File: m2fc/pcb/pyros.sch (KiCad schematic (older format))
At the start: 48 parts, among them P601 CONN_2, P602 CONN_2, P603 CONN_2, Q601 MOSFET_P, Q602 MOSFET_N, Q603 MOSFET_P, Q604 MOSFET_N, Q605 MOSFET_P, Q606 MOSFET_N, U601 HOUSING, U602 HOUSING, U603 HOUSING

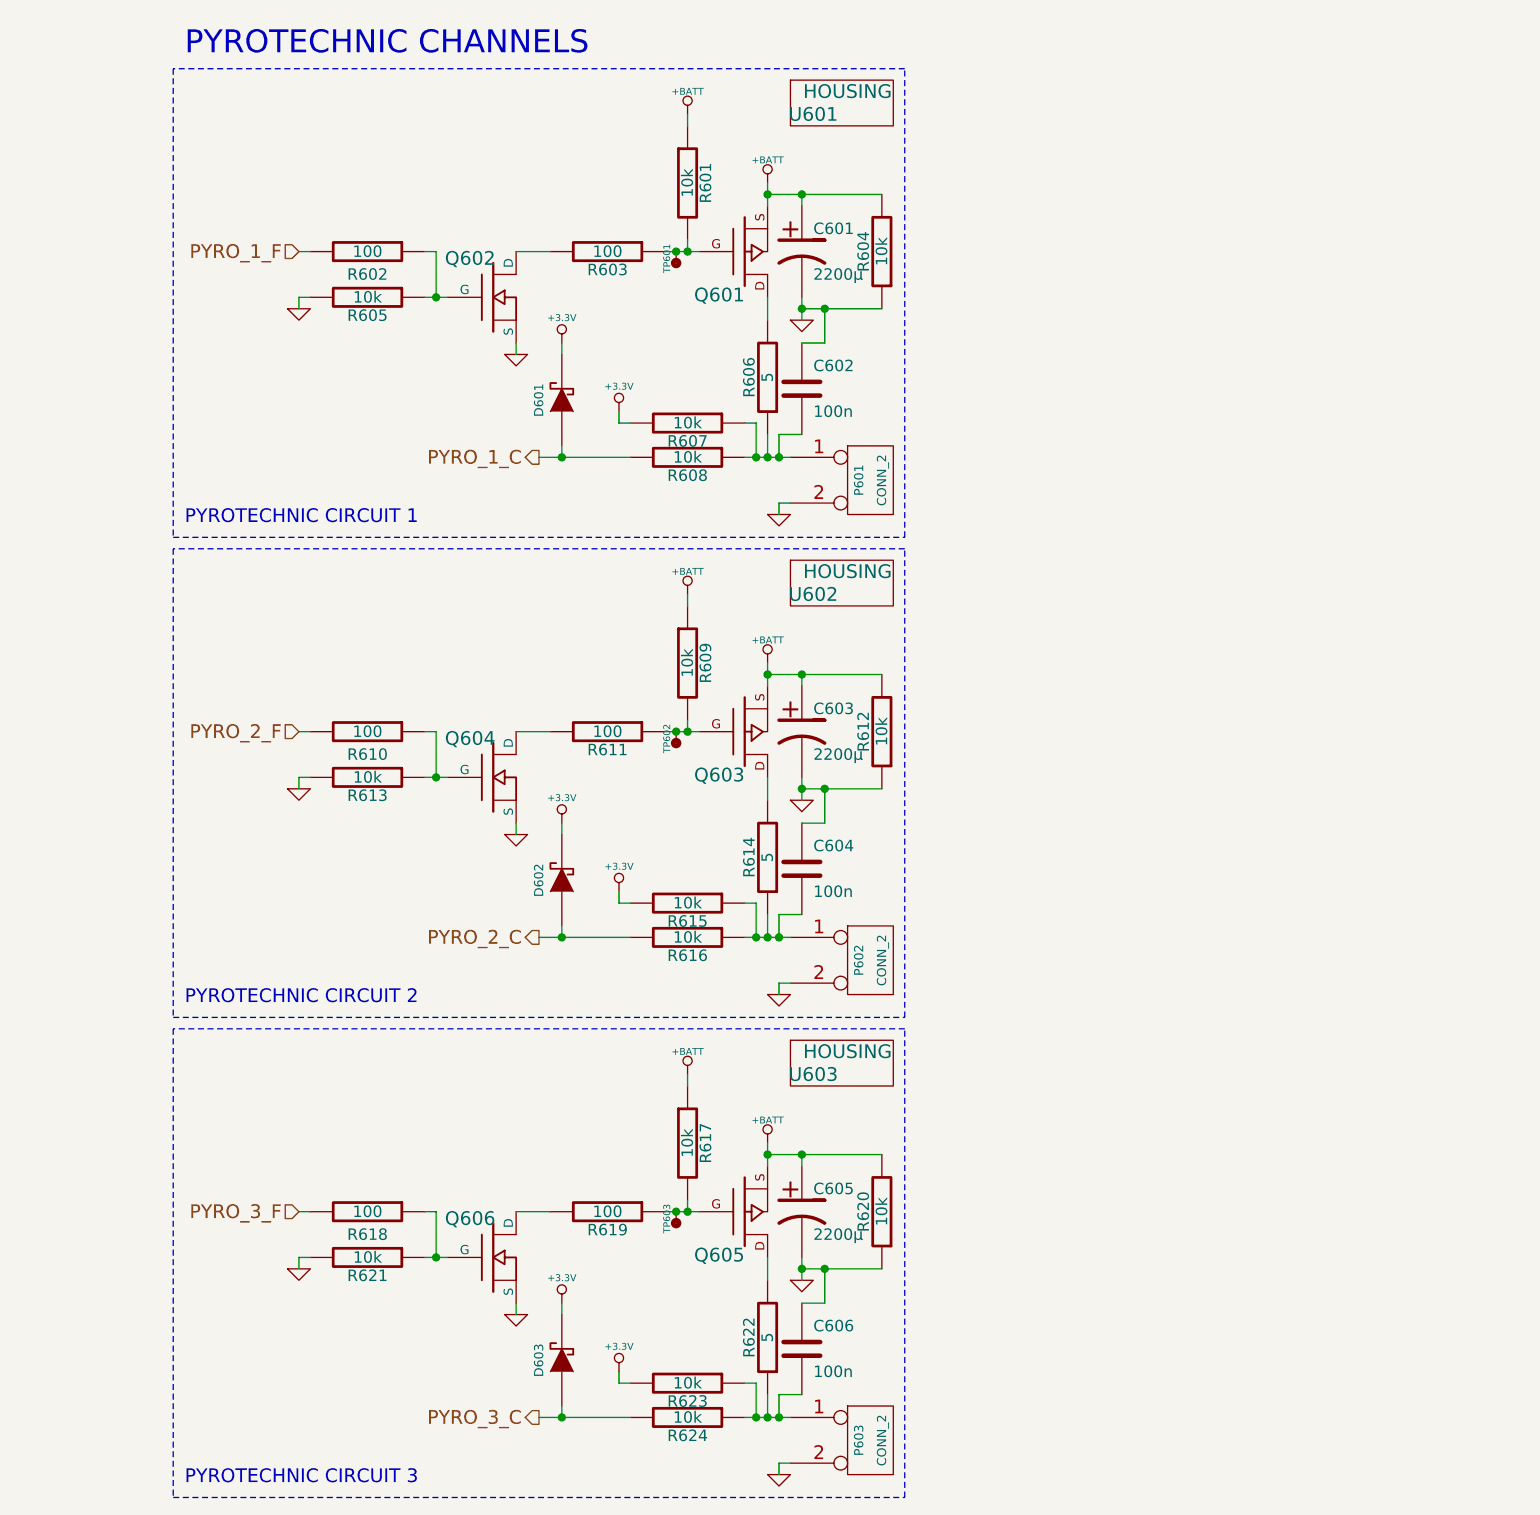
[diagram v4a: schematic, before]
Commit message: sd pullups, shielded sgs
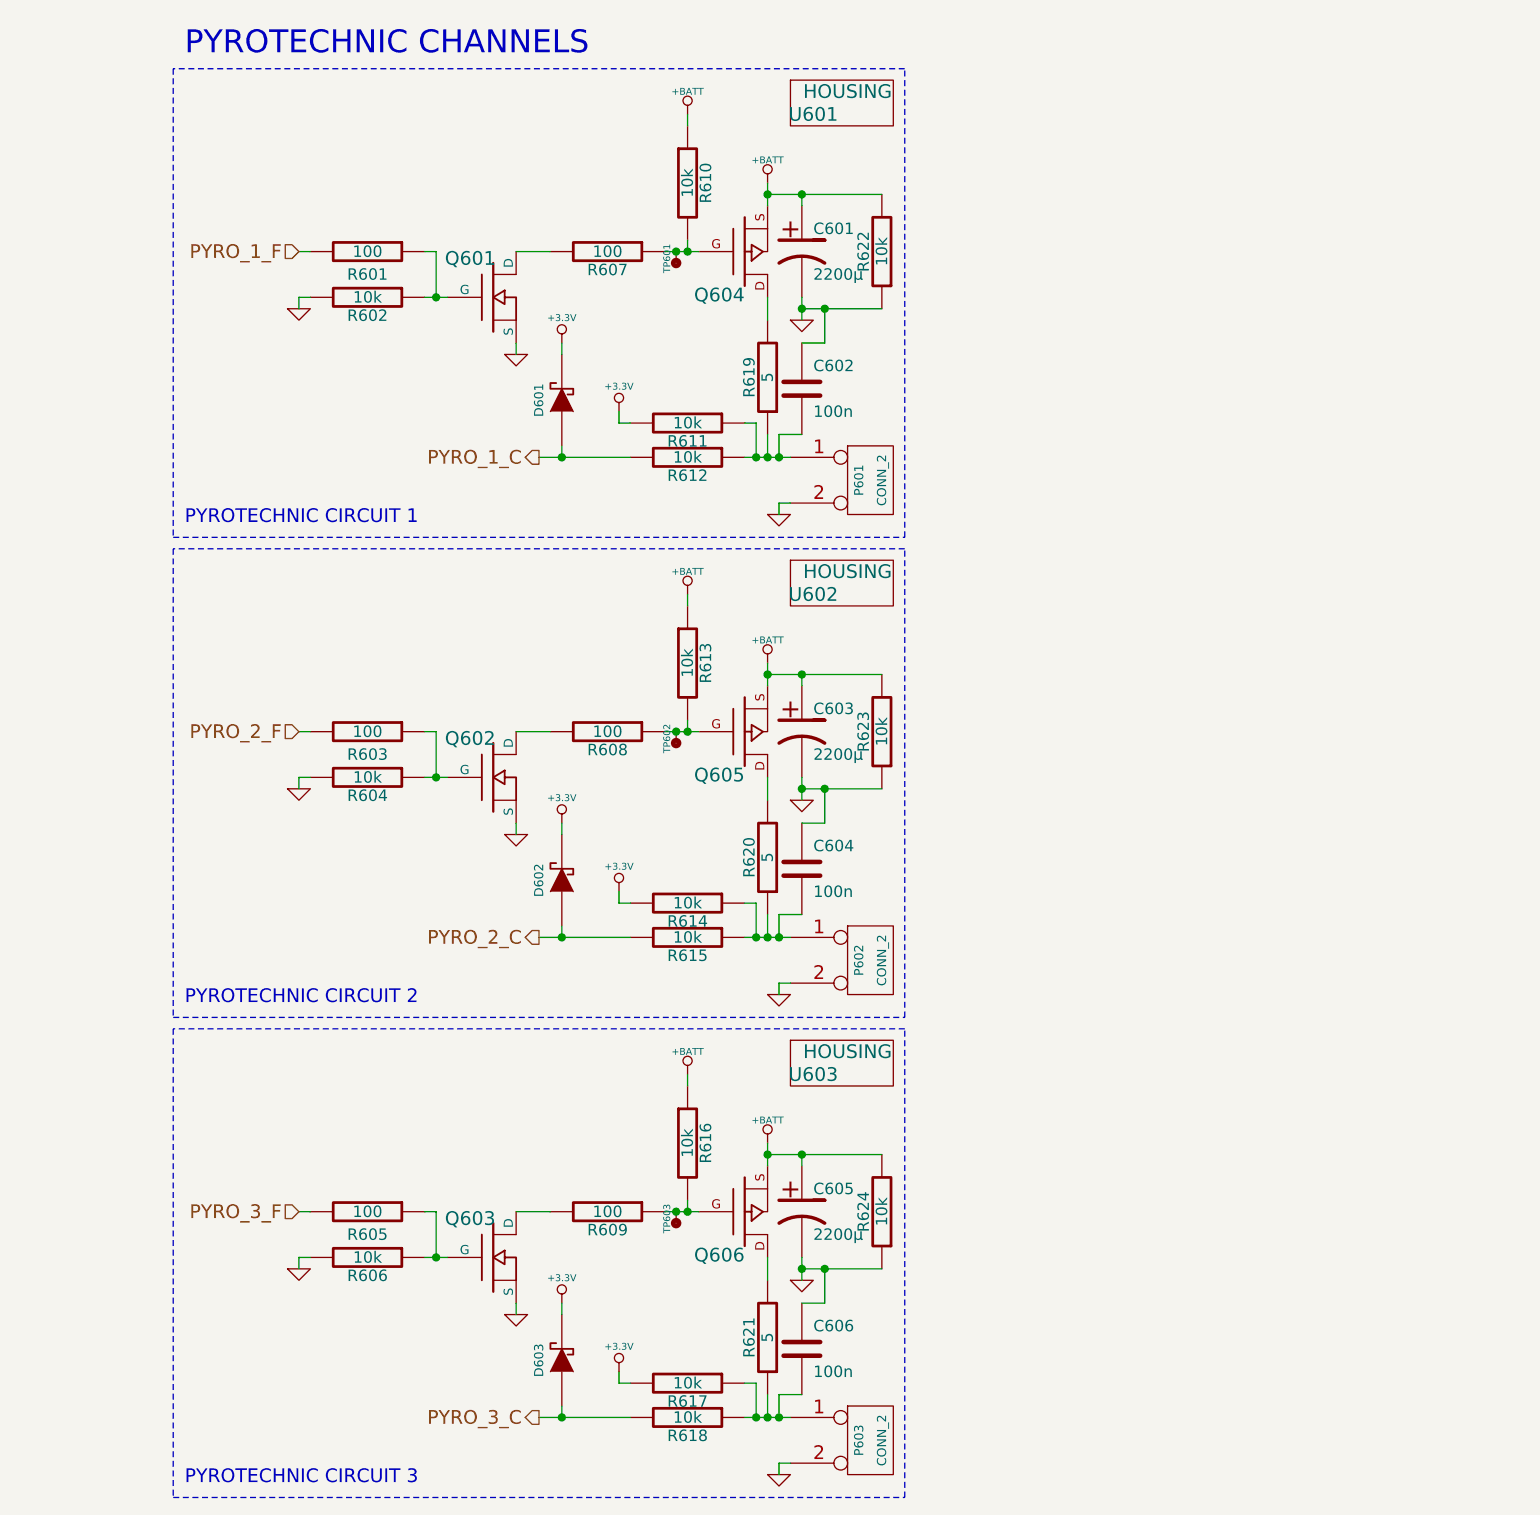
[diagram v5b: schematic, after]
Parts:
- C602, C604, C606: footprint 0603 -> m2fc:C0603
- P601, P602, P603: footprint (none) -> m2fc:S02B-PASK-2
- R601: renamed from R602; footprint 0603 -> m2fc:R0603
- R602: renamed from R605; footprint 0603 -> m2fc:R0603
- R603: renamed from R610; footprint 0603 -> m2fc:R0603
- R604: renamed from R613; footprint 0603 -> m2fc:R0603
- R605: renamed from R618; footprint 0603 -> m2fc:R0603
- R606: renamed from R621; footprint 0603 -> m2fc:R0603
- R607: renamed from R603; footprint 0603 -> m2fc:R0603
- R608: renamed from R611; footprint 0603 -> m2fc:R0603
- R609: renamed from R619; footprint 0603 -> m2fc:R0603
- R610: renamed from R601; footprint 0603 -> m2fc:R0603
- R611: renamed from R607; footprint 0603 -> m2fc:R0603
- R612: renamed from R608; footprint 0603 -> m2fc:R0603
- R613: renamed from R609; footprint 0603 -> m2fc:R0603
- R614: renamed from R615; footprint 0603 -> m2fc:R0603
- R615: renamed from R616; footprint 0603 -> m2fc:R0603
- R616: renamed from R617; footprint 0603 -> m2fc:R0603
- R617: renamed from R623; footprint 0603 -> m2fc:R0603
- R618: renamed from R624; footprint 0603 -> m2fc:R0603
- R622: renamed from R604; footprint 0603 -> m2fc:R0603
- R623: renamed from R612; footprint 0603 -> m2fc:R0603
- R624: renamed from R620; footprint 0603 -> m2fc:R0603
- TP601, TP602, TP603: footprint (none) -> m2fc:TESTPAD
- renumbered Q602 to Q601, Q604 to Q602, Q606 to Q603, Q601 to Q604, Q603 to Q605, Q605 to Q606, R606 to R619, R614 to R620, R622 to R621

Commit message: add esd diodes to m2fc
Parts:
- added D502, D504, D506: CGA0402MLC-12G, m2fc:R0402, symbol CGA0402MLC-12G
- renumbered C601 to C501, C602 to C502, C603 to C503, C604 to C504, C605 to C505, C606 to C506, D601 to D501, D602 to D503, D603 to D505, P601 to P501, P602 to P502, P603 to P503, Q604 to Q501, Q601 to Q502, Q605 to Q503, Q602 to Q504, Q606 to Q505, Q603 to Q506, R610 to R501, R601 to R502, R607 to R503, R622 to R504, R602 to R505, R619 to R506, R611 to R507, R612 to R508, R613 to R509, R603 to R510, R608 to R511, R623 to R512, R604 to R513, R620 to R514, R614 to R515, R615 to R516, R616 to R517, R605 to R518, R609 to R519, R624 to R520, R606 to R521, R621 to R522, R617 to R523, R618 to R524, TP601 to TP501, TP602 to TP502, TP603 to TP503, U601 to U501, U602 to U502, U603 to U503
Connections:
- net GND: now also D502.2, D504.2, D506.2
- net at C502.2, P501.1 (P1), R506.1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: now also D502.1
- net at C504.2, P502.1 (P1), R514.1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: now also D504.1
- net at C506.2, P503.1 (P1), R522.1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: now also D506.1
